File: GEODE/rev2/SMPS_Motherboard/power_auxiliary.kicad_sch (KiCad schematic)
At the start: 47 parts, among them IC1201 MAX25262AFOF_VY+, IC801 TPS629206QDRLRQ1, Q801 PMV90ENER, Q802 PMV90ENER, U801 TPS2116DRLR, U802 LMR36506MSC5RPERQ1

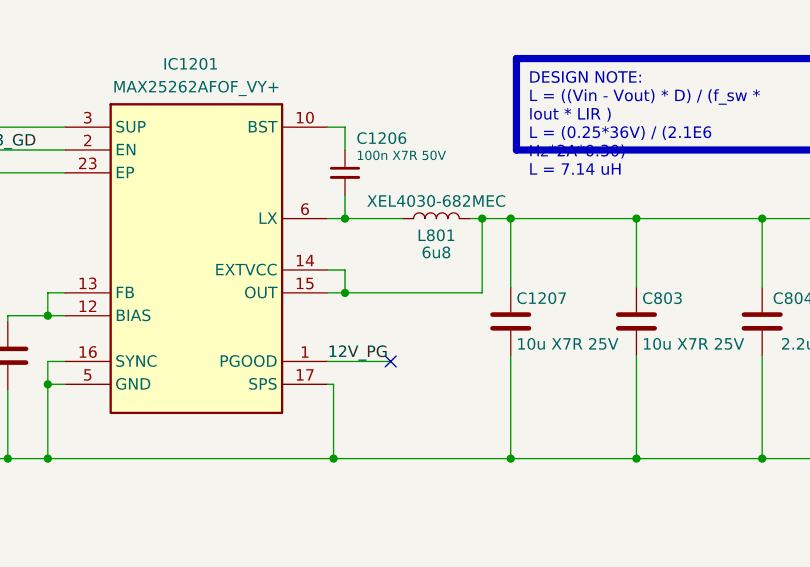
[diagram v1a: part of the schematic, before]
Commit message: changed connectors, removed can, added fuse, disconnected EXTVCC in power generation
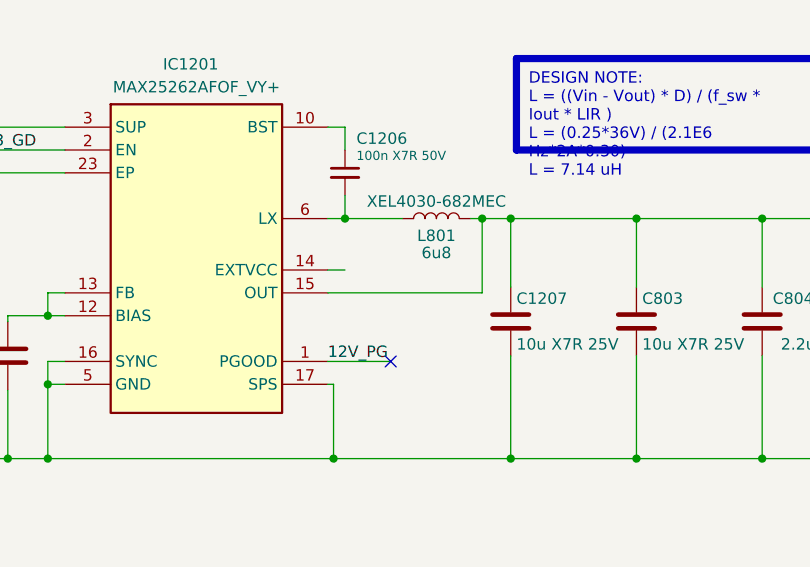
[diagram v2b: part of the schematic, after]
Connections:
- net +12V: no longer IC1201.14 (EXTVCC)
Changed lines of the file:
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@@
-	)
-	(junction
-		(at 187.325 135.89)
-		(diameter 0)
-		(color 0 0 0 0)
 	)
 	(junction
@@
 	(wire
 		(pts
-			(xy 187.325 135.89) (xy 202.565 135.89)
+			(xy 185.42 135.89) (xy 202.565 135.89)
 		)
 		(stroke
@@
 	(wire
 		(pts
-			(xy 187.325 133.35) (xy 187.325 135.89)
-		)
-		(stroke
-			(width 0)
-			(type default)
-		)
-	)
-	(wire
-		(pts
 			(xy 226.695 67.945) (xy 226.695 79.375)
 		)
@@
 		)
 		(stroke
-			(width 0)
-			(type default)
-		)
-	)
-	(wire
-		(pts
-			(xy 185.42 135.89) (xy 187.325 135.89)
-		)
-		(stroke

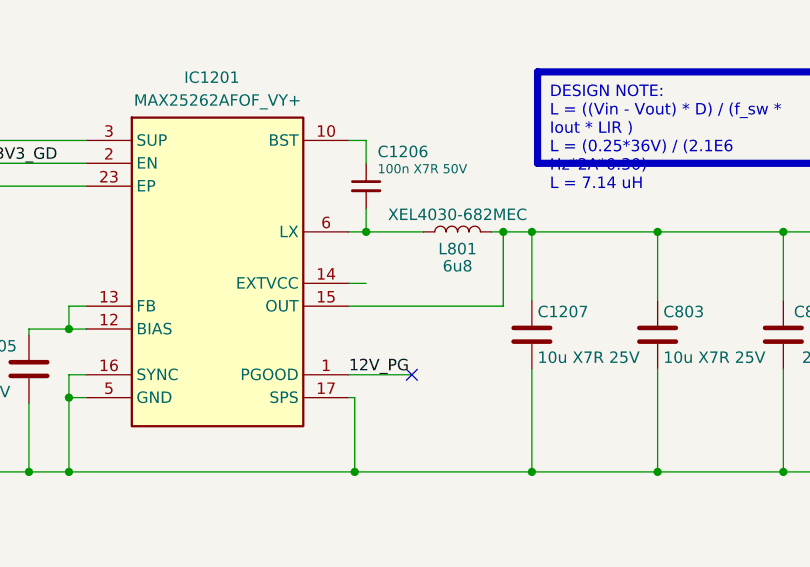
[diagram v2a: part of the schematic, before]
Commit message: replaced output connectors, added UART connector, removed fuse - schematics
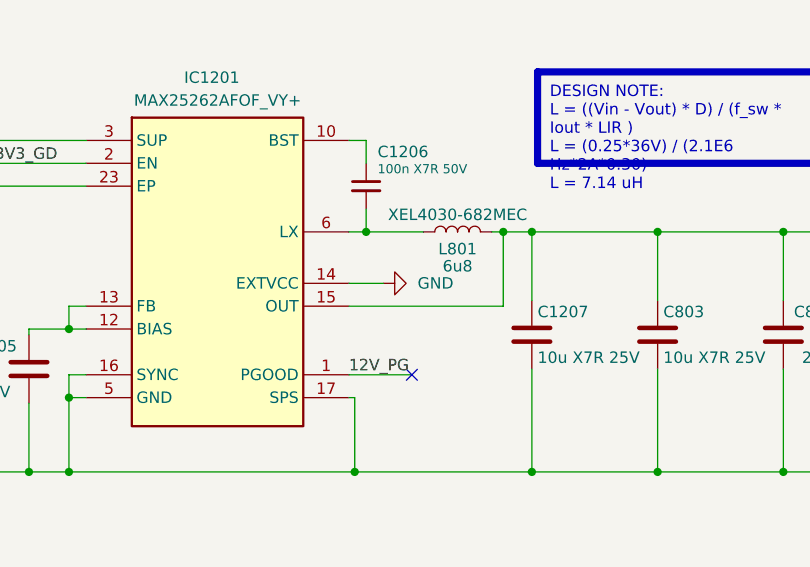
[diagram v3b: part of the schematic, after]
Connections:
- net GND: now also IC1201.14 (EXTVCC)
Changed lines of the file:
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@@
 	(wire
 		(pts
-			(xy 185.42 133.35) (xy 187.325 133.35)
+			(xy 185.42 133.35) (xy 189.23 133.35)
 		)
 		(stroke
@@
 					(unit 1)
 				)
+			)
+		)
+	)
+	(symbol
+		(lib_name "GND_1")
+		(lib_id "power:GND")
+		(at 189.23 133.35 90)
+		(unit 1)
+		(exclude_from_sim no)
+		(in_bom yes)
+		(on_board yes)
+		(dnp no)
+		(fields_autoplaced yes)
+		(property "Reference" "#PWR02"
+			(at 195.58 133.35 0)
+			(effects
+				(font
+					(size 1.27 1.27)
+				)
+				(hide yes)
+			)
+		)
+		(property "Value" "GND"
+			(at 193.04 133.3499 90)
+			(effects
+				(font
+					(size 1.27 1.27)
+				)
+				(justify right)
+			)
+		)
+		(property "Footprint" ""
+			(at 189.23 133.35 0)
+			(effects
+				(font
+					(size 1.27 1.27)
+				)
+				(hide yes)
+			)
+		)
+		(property "Datasheet" ""
+			(at 189.23 133.35 0)
+			(effects
+				(font
+					(size 1.27 1.27)
+				)
+				(hide yes)
+			)
+		)
+		(property "Description" "Power symbol creates a global label with name \"GND\" , ground"
+			(at 189.23 133.35 0)
+			(effects
+				(font
+					(size 1.27 1.27)
+				)
+				(hide yes)
+			)
+		)
+		(pin "1"
+		)
+		(instances
+			(project ""
+				(path "/0650c7a8-acba-429c-9f8e-eec0baf0bc1c/fede4c36-00cc-4d3d-b71c-5243ba232202/90980504-ca7e-4d0f-ada1-af3b0bda141f"
+					(reference "#PWR02")
+					(unit 1)
+				)
